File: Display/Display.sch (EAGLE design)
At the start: 27 parts, among them SW1 SWITCH-PTS-810, SW2 SWITCH-PTS-810, SW3 SWITCH-PTS-810, U1 ER-OLED0.95-2C, U2 FAN5331SX, U3 ATSAMD20E17A-AU, U4 MIC5205-3.3YM5 TR

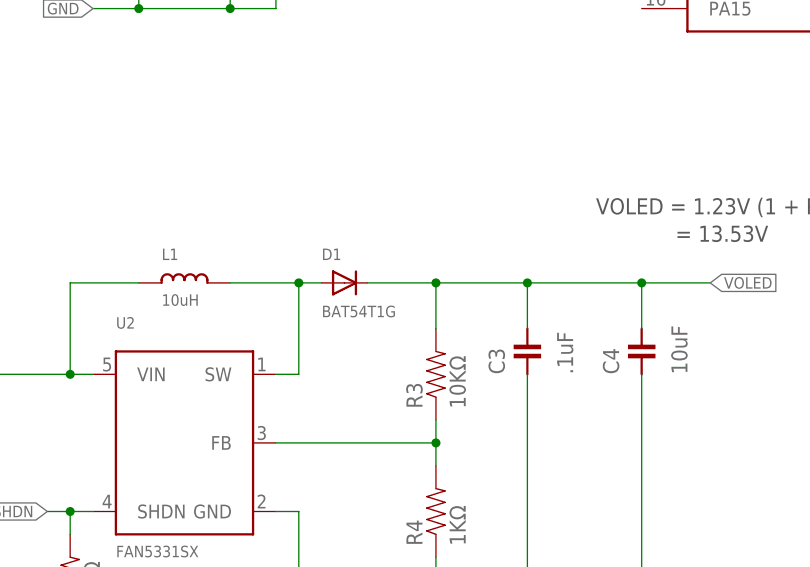
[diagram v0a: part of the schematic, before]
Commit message: New diode selections
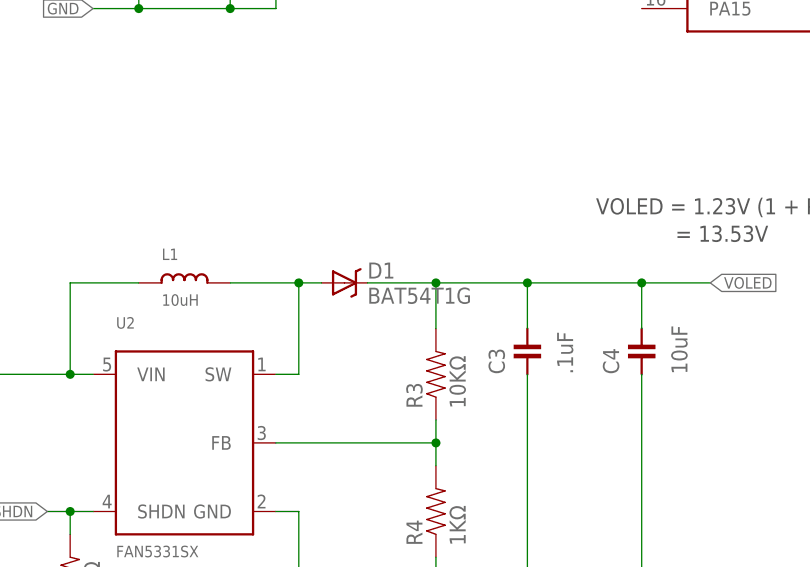
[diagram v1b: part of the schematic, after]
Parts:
- D1: device microbuilder:DIODESOD-123 -> Modulo:DIODE-SCHOTTKY; PARTNUM BAT54T1G -> (none)
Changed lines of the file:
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@@
 <attribute name="PARTNUM" value="MPI2520R1-100-R"/>
 </part>
-<part name="D1" library="microbuilder" deviceset="DIODE" device="SOD-123" value="BAT54T1G">
-<attribute name="PARTNUM" value="BAT54T1G"/>
-</part>
+<part name="D1" library="Modulo" deviceset="DIODE-SCHOTTKY" device="" value="BAT54T1G"/>
 <part name="R3" library="Modulo" deviceset="RESISTOR" device="-10KΩ" value="10KΩ"/>
 <part name="R4" library="Modulo" deviceset="RESISTOR" device="-1KΩ" value="1KΩ"/>

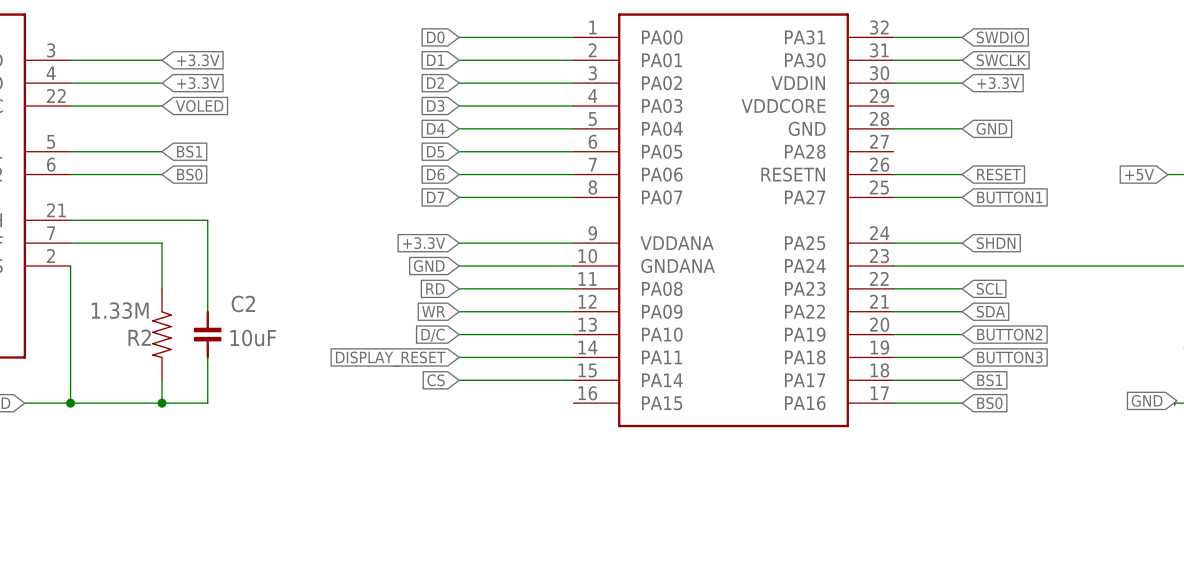
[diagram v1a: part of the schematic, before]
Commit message: Fixed a missing connection.
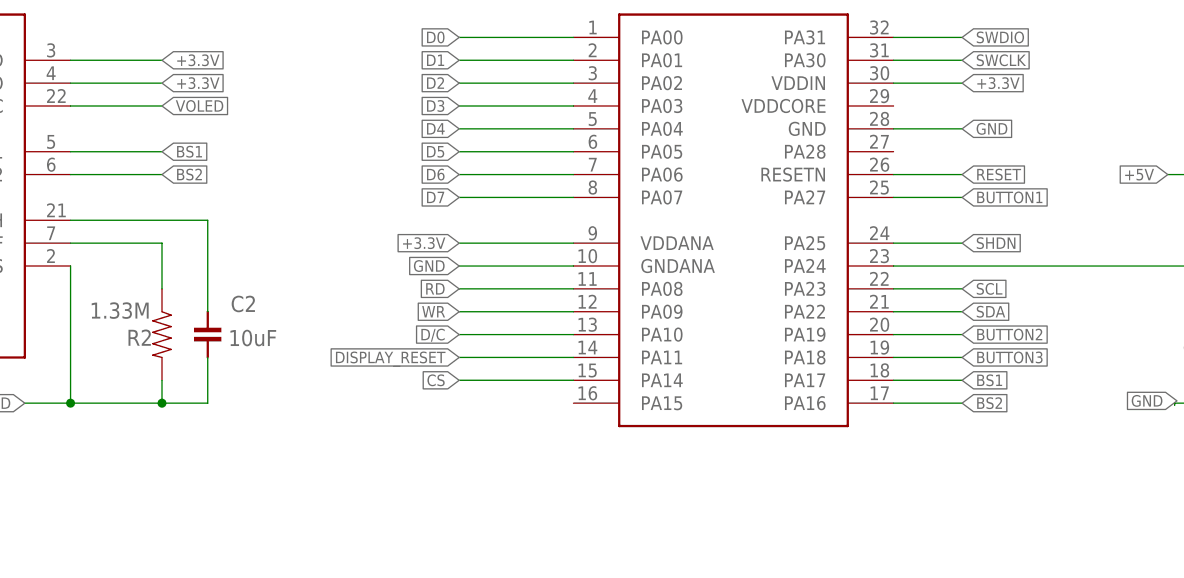
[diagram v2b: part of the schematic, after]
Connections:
- net BS0 renamed BS2
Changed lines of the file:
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@@
 </segment>
 </net>
-<net name="BS0" class="0">
+<net name="BS2" class="0">
 <segment>
 <pinref part="U1" gate="G$1" pin="BS2"/>

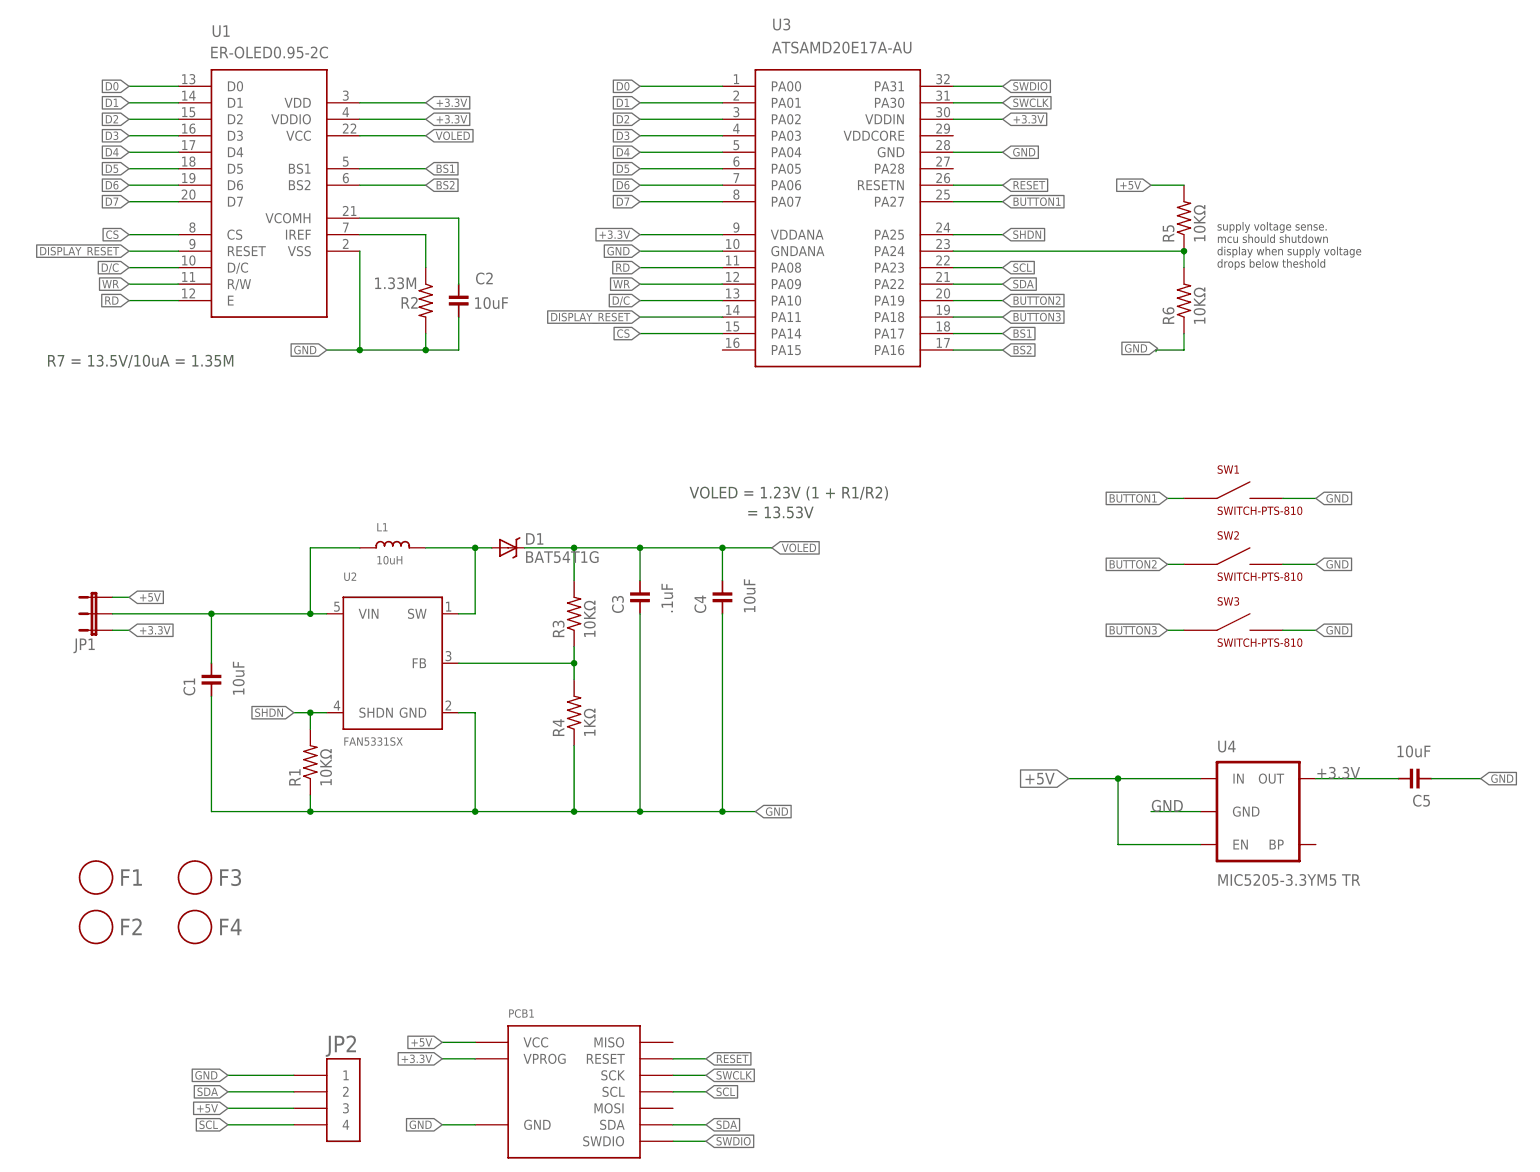
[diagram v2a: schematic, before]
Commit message: Check point of current PCB designs. Among other things I think this change includes rewiring of programming lines on many of the boards,.
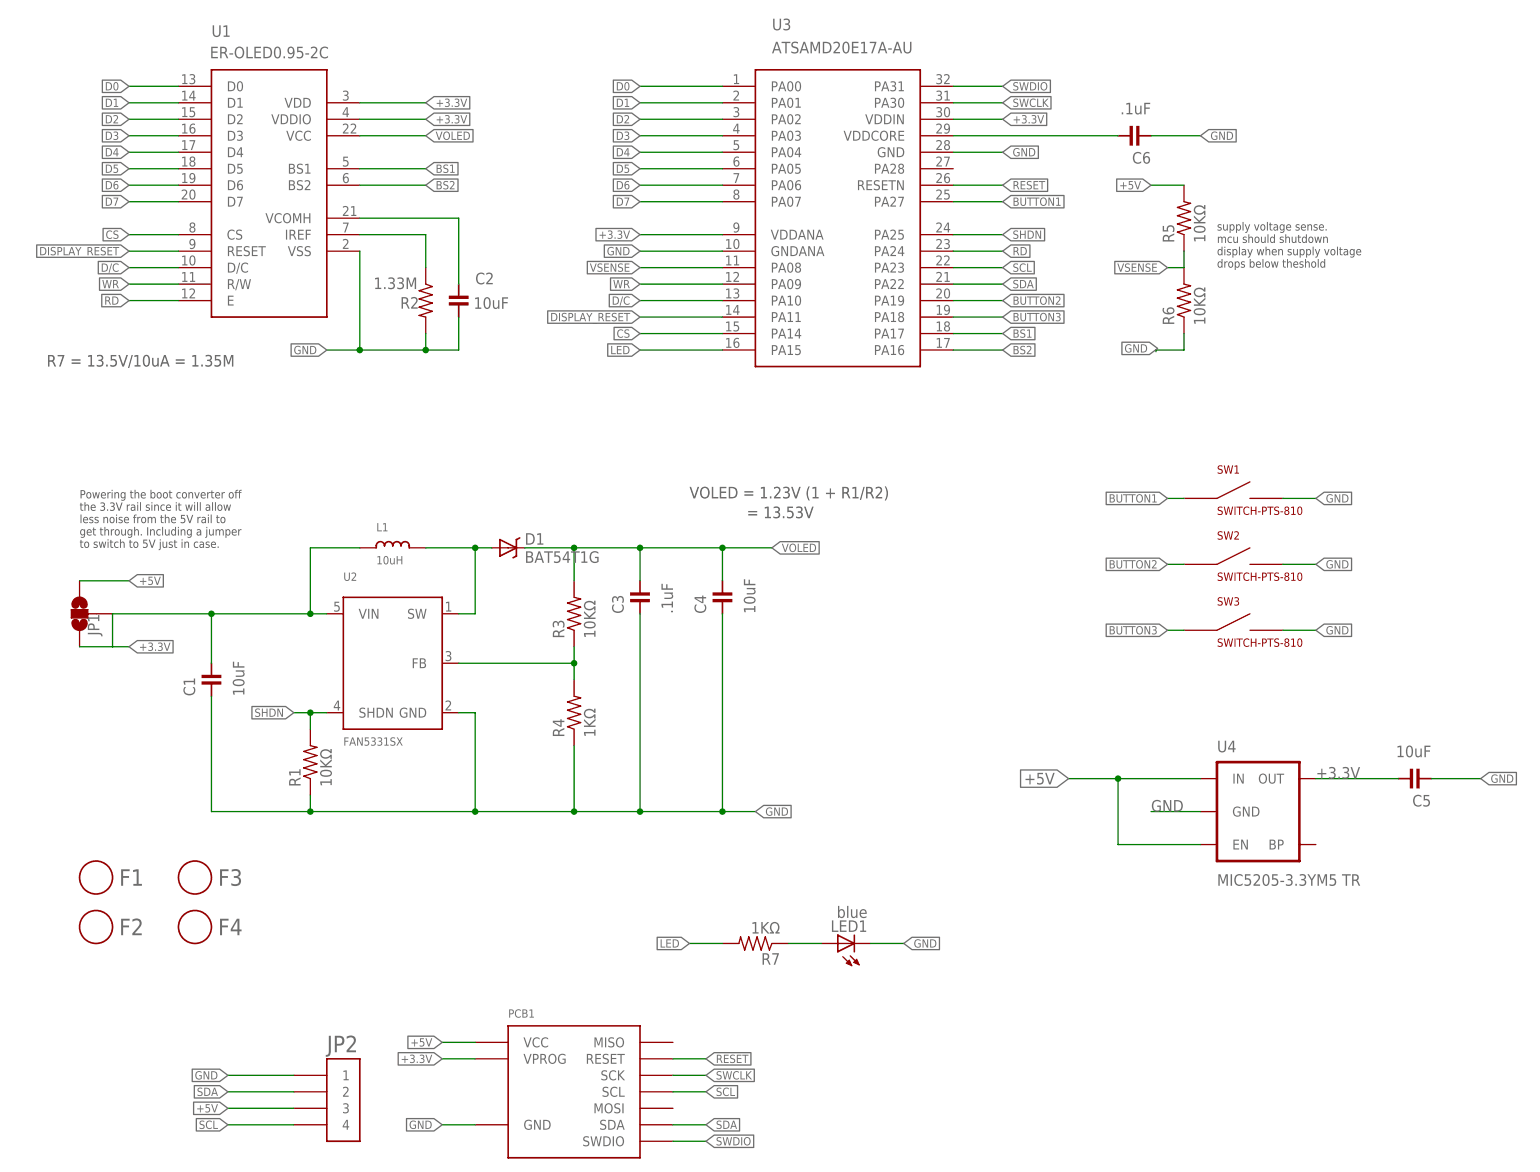
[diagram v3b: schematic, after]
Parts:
- added C6: .1uF, Modulo:CAPACITOR-.1UF
- added LED1: blue, Modulo:LED-0805-BLUE
- added R7: 1KΩ, Modulo:RESISTOR-1KΩ
- JP1: value JUMPER-31-2 -> (none); device SparkFun-Passives:JUMPER-31-2 -> SparkFun-Passives:SOLDERJUMPER_2WAYS
- JP2: PARTNUM (none) -> 147721-3
- PCB1: VERSION 2 -> 3
- U3: PARTNUM SAMD20E17A -> ATSAMD20E17A-AU
- U4: PARTNUM MIC5205-3.3YM5 -> MIC5205-3.3YM5 TR
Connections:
- removed net VIN: C1.1, JP1.2, L1.1, U2.VIN
- new net LED: R7.2, U3.PA15
- new net N$4: C6.1, U3.VDDCORE
- new net N$6: LED1.A, R7.1
- net +3.3V: now also C1.1, JP1.2, L1.1, U2.VIN
- net GND: now also C6.2, LED1.C
- net RD: now also U3.PA24; no longer U3.PA08
- net VSENSE: now also U3.PA08; no longer U3.PA24
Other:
- note added: "Powering the boot converter off the 3.3V rail since it will allow less noise from the 5V rail to get through. Including a jumper to switch to 5V just in case."
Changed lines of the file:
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@@
 <parts>
 <part name="U4" library="Modulo" deviceset="VREG-MIC5205" device="-3.3V" value="MIC5205-3.3YM5 TR">
-<attribute name="PARTNUM" value="MIC5205-3.3YM5"/>
+<attribute name="PARTNUM" value="MIC5205-3.3YM5 TR"/>
 </part>
 <part name="PCB1" library="Modulo" deviceset="DEVICE-PCB" device="" value="DEVICE-PCB">
 <attribute name="BOARD" value="Display"/>
 <attribute name="PARTNUM" value="Display PCB"/>
-<attribute name="VERSION" value="2"/>
+<attribute name="VERSION" value="3"/>
 </part>
 <part name="SW1" library="Modulo" deviceset="SWITCH" device="-PTS-810" value="SWITCH-PTS-810"/>
@@
 <part name="SW3" library="Modulo" deviceset="SWITCH" device="-PTS-810" value="SWITCH-PTS-810"/>
 <part name="U3" library="Modulo" deviceset="SAMD21E" device="" value="ATSAMD20E17A-AU">
-<attribute name="PARTNUM" value="SAMD20E17A"/>
+<attribute name="PARTNUM" value="ATSAMD20E17A-AU"/>
 </part>
 <part name="U1" library="Modulo" deviceset="OLED-COLOR" device="REVERSE" value="ER-OLED0.95-2C">
@@
 <part name="R3" library="Modulo" deviceset="RESISTOR" device="-10KΩ" value="10KΩ"/>
 <part name="R4" library="Modulo" deviceset="RESISTOR" device="-1KΩ" value="1KΩ"/>
-<part name="JP2" library="Modulo" deviceset="HEADER-1X4" device="-AMPMODU"/>
+<part name="JP2" library="Modulo" deviceset="HEADER-1X4" device="-AMPMODU">
+<attribute name="PARTNUM" value="147721-3"/>
+</part>
 <part name="R1" library="Modulo" deviceset="RESISTOR" device="-10KΩ" value="10KΩ"/>
 <part name="R5" library="Modulo" deviceset="RESISTOR" device="-10KΩ" value="10KΩ"/>
@@
 <part name="C5" library="Modulo" deviceset="CAPACITOR" device="-10UF" value="10uF"/>
 <part name="C4" library="Modulo" deviceset="CAPACITOR" device="-10UF" value="10uF"/>
-<part name="JP1" library="SparkFun-Passives" deviceset="JUMPER-3" device="1-2">
+<part name="JP1" library="SparkFun-Passives" deviceset="SOLDERJUMPER_2WAY" device="S">
 <attribute name="BOM" value="EXCLUDE"/>
 </part>
@@
 <part name="F3" library="Modulo" deviceset="FIDUCIAL" device=""/>
 <part name="F4" library="Modulo" deviceset="FIDUCIAL" device=""/>
+<part name="LED1" library="Modulo" deviceset="LED" device="-0805-BLUE" value="blue"/>
+<part name="R7" library="Modulo" deviceset="RESISTOR" device="-1KΩ" value="1KΩ"/>
+<part name="C6" library="Modulo" deviceset="CAPACITOR" device="-.1UF" value=".1uF"/>
 </parts>
 <sheets>
@@
 display when supply voltage
 drops below theshold</text>
+<text x="12.7" y="101.6" size="1.27" layer="97">Powering the boot converter off
+the 3.3V rail since it will allow
+less noise from the 5V rail to
+get through. Including a jumper
+to switch to 5V just in case.</text>
 </plain>
 <instances>
@@
 <instance part="C5" gate="G$1" x="218.44" y="66.04" rot="R90"/>
 <instance part="C4" gate="G$1" x="111.76" y="93.98"/>
-<instance part="JP1" gate="G$1" x="15.24" y="88.9" smashed="yes" rot="R90">
-<attribute name="NAME" x="15.24" y="87.63" size="1.778" layer="95" rot="R180"/>
-<attribute name="BOM" x="15.24" y="88.9" size="1.27" layer="96" rot="R90" display="off"/>
+<instance part="JP1" gate="G$1" x="12.7" y="91.44" smashed="yes" rot="R180">
+<attribute name="NAME" x="13.97" y="91.44" size="1.778" layer="95" rot="R270"/>
+<attribute name="BOM" x="12.7" y="91.44" size="1.27" layer="96" rot="R180" display="off"/>
 </instance>
 <instance part="F1" gate="G$1" x="15.24" y="50.8"/>
@@
 <instance part="F3" gate="G$1" x="30.48" y="50.8"/>
 <instance part="F4" gate="G$1" x="30.48" y="43.18"/>
+<instance part="LED1" gate="G$1" x="129.54" y="40.64" rot="R90"/>
+<instance part="R7" gate="G$1" x="116.84" y="40.64" rot="R180"/>
+<instance part="C6" gate="G$1" x="175.26" y="165.1" rot="R90"/>
 </instances>
 <busses>
@@
 <label x="178.816" y="132.334" size="1.27" layer="95" rot="R180" xref="yes"/>
 </segment>
+<segment>
+<pinref part="LED1" gate="G$1" pin="C"/>
+<wire x1="134.62" y1="40.64" x2="139.7" y2="40.64" width="0.1524" layer="91"/>
+<label x="139.7" y="40.64" size="1.27" layer="95" xref="yes"/>
+</segment>
+<segment>
+<pinref part="C6" gate="G$1" pin="2"/>
+<wire x1="177.8" y1="165.1" x2="185.42" y2="165.1" width="0.1524" layer="91"/>
+<label x="185.42" y="165.1" size="1.27" layer="95" xref="yes"/>
+</segment>
 </net>
 <net name="+3.3V" class="0">
@@
 </segment>
 <segment>
+<wire x1="33.02" y1="91.44" x2="33.02" y2="83.82" width="0.1524" layer="91"/>
+<wire x1="50.8" y1="91.44" x2="48.26" y2="91.44" width="0.1524" layer="91"/>
+<wire x1="48.26" y1="91.44" x2="33.02" y2="91.44" width="0.1524" layer="91"/>
+<wire x1="48.26" y1="91.44" x2="48.26" y2="101.6" width="0.1524" layer="91"/>
+<wire x1="48.26" y1="101.6" x2="55.88" y2="101.6" width="0.1524" layer="91"/>
+<junction x="48.26" y="91.44"/>
+<pinref part="U2" gate="G$1" pin="VIN"/>
+<pinref part="L1" gate="G$1" pin="1"/>
+<pinref part="C1" gate="G$1" pin="1"/>
+<pinref part="JP1" gate="G$1" pin="2"/>
+<wire x1="17.78" y1="91.44" x2="33.02" y2="91.44" width="0.1524" layer="91"/>
+<junction x="33.02" y="91.44"/>
 <pinref part="JP1" gate="G$1" pin="1"/>
-<wire x1="17.78" y1="88.9" x2="20.32" y2="88.9" width="0.1524" layer="91"/>
-<label x="20.32" y="88.9" size="1.27" layer="95" xref="yes"/>
+<wire x1="12.7" y1="86.36" x2="17.78" y2="86.36" width="0.1524" layer="91"/>
+<label x="20.32" y="86.36" size="1.27" layer="95" xref="yes"/>
+<wire x1="17.78" y1="86.36" x2="20.32" y2="86.36" width="0.1524" layer="91"/>
+<wire x1="17.78" y1="91.44" x2="17.78" y2="86.36" width="0.1524" layer="91"/>
 </segment>
 </net>
@@
 <segment>
 <pinref part="JP1" gate="G$1" pin="3"/>
-<wire x1="17.78" y1="93.98" x2="20.32" y2="93.98" width="0.1524" layer="91"/>
-<label x="20.32" y="93.98" size="1.27" layer="95" xref="yes"/>
+<wire x1="12.7" y1="96.52" x2="20.32" y2="96.52" width="0.1524" layer="91"/>
+<label x="20.32" y="96.52" size="1.27" layer="95" xref="yes"/>
 </segment>
 </net>
@@
 </segment>
 <segment>
-<pinref part="U3" gate="G$1" pin="PA08"/>
-<wire x1="111.76" y1="144.78" x2="99.06" y2="144.78" width="0.1524" layer="91"/>
-<label x="99.06" y="144.78" size="1.27" layer="95" rot="R180" xref="yes"/>
+<pinref part="U3" gate="G$1" pin="PA24"/>
+<wire x1="147.32" y1="147.32" x2="154.94" y2="147.32" width="0.1524" layer="91"/>
+<label x="154.94" y="147.32" size="1.27" layer="95" xref="yes"/>
 </segment>
 </net>
@@
 <net name="VSENSE" class="0">
 <segment>
-<pinref part="U3" gate="G$1" pin="PA24"/>
 <pinref part="R5" gate="G$1" pin="1"/>
 <pinref part="R6" gate="G$1" pin="2"/>
 <wire x1="182.88" y1="147.32" x2="182.88" y2="144.78" width="0.1524" layer="91"/>
-<wire x1="147.32" y1="147.32" x2="182.88" y2="147.32" width="0.1524" layer="91"/>
-<junction x="182.88" y="147.32"/>
-</segment>
-</net>
-<net name="VIN" class="0">
-<segment>
-<wire x1="33.02" y1="91.44" x2="33.02" y2="83.82" width="0.1524" layer="91"/>
-<wire x1="50.8" y1="91.44" x2="48.26" y2="91.44" width="0.1524" layer="91"/>
-<wire x1="48.26" y1="91.44" x2="33.02" y2="91.44" width="0.1524" layer="91"/>
-<wire x1="48.26" y1="91.44" x2="48.26" y2="101.6" width="0.1524" layer="91"/>
-<wire x1="48.26" y1="101.6" x2="55.88" y2="101.6" width="0.1524" layer="91"/>
-<junction x="48.26" y="91.44"/>
-<pinref part="U2" gate="G$1" pin="VIN"/>
-<pinref part="L1" gate="G$1" pin="1"/>
-<pinref part="C1" gate="G$1" pin="1"/>
-<pinref part="JP1" gate="G$1" pin="2"/>
-<wire x1="17.78" y1="91.44" x2="33.02" y2="91.44" width="0.1524" layer="91"/>
-<junction x="33.02" y="91.44"/>
-</segment>
-</net>
+<wire x1="182.88" y1="144.78" x2="180.34" y2="144.78" width="0.1524" layer="91"/>
+<label x="180.34" y="144.78" size="1.27" layer="95" rot="R180" xref="yes"/>
+</segment>
+<segment>
+<pinref part="U3" gate="G$1" pin="PA08"/>
+<wire x1="111.76" y1="144.78" x2="99.06" y2="144.78" width="0.1524" layer="91"/>
+<label x="99.06" y="144.78" size="1.27" layer="95" rot="R180" xref="yes"/>
+</segment>
+</net>
+<net name="N$6" class="0">
+<segment>
+<pinref part="LED1" gate="G$1" pin="A"/>
+<pinref part="R7" gate="G$1" pin="1"/>
+<wire x1="127" y1="40.64" x2="121.92" y2="40.64" width="0.1524" layer="91"/>
+</segment>
+</net>
+<net name="LED" class="0">
+<segment>
+<pinref part="R7" gate="G$1" pin="2"/>
+<wire x1="111.76" y1="40.64" x2="106.68" y2="40.64" width="0.1524" layer="91"/>
+<label x="106.68" y="40.64" size="1.27" layer="95" rot="R180" xref="yes"/>
+</segment>
+<segment>
+<pinref part="U3" gate="G$1" pin="PA15"/>
+<wire x1="111.76" y1="132.08" x2="99.06" y2="132.08" width="0.1524" layer="91"/>
+<label x="99.06" y="132.08" size="1.27" layer="95" rot="R180" xref="yes"/>
+</segment>
+</net>
+<net name="N$4" class="0">
+<segment>
+<pinref part="U3" gate="G$1" pin="VDDCORE"/>
+<wire x1="147.32" y1="165.1" x2="172.72" y2="165.1" width="0.1524" layer="91"/>
+<pinref part="C6" gate="G$1" pin="1"/>
+</segment>
+</net>
